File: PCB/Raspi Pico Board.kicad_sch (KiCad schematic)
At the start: 0 parts

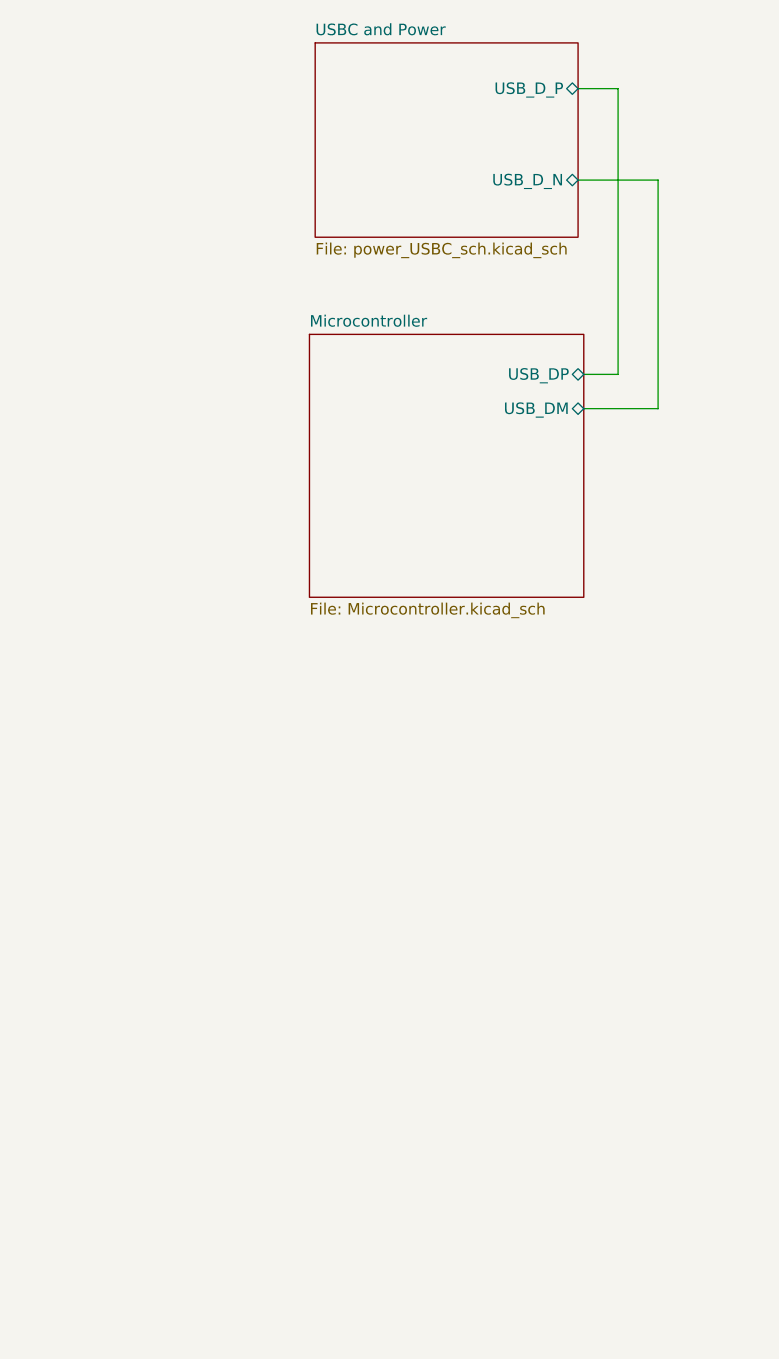
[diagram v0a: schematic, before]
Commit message: New sheet added
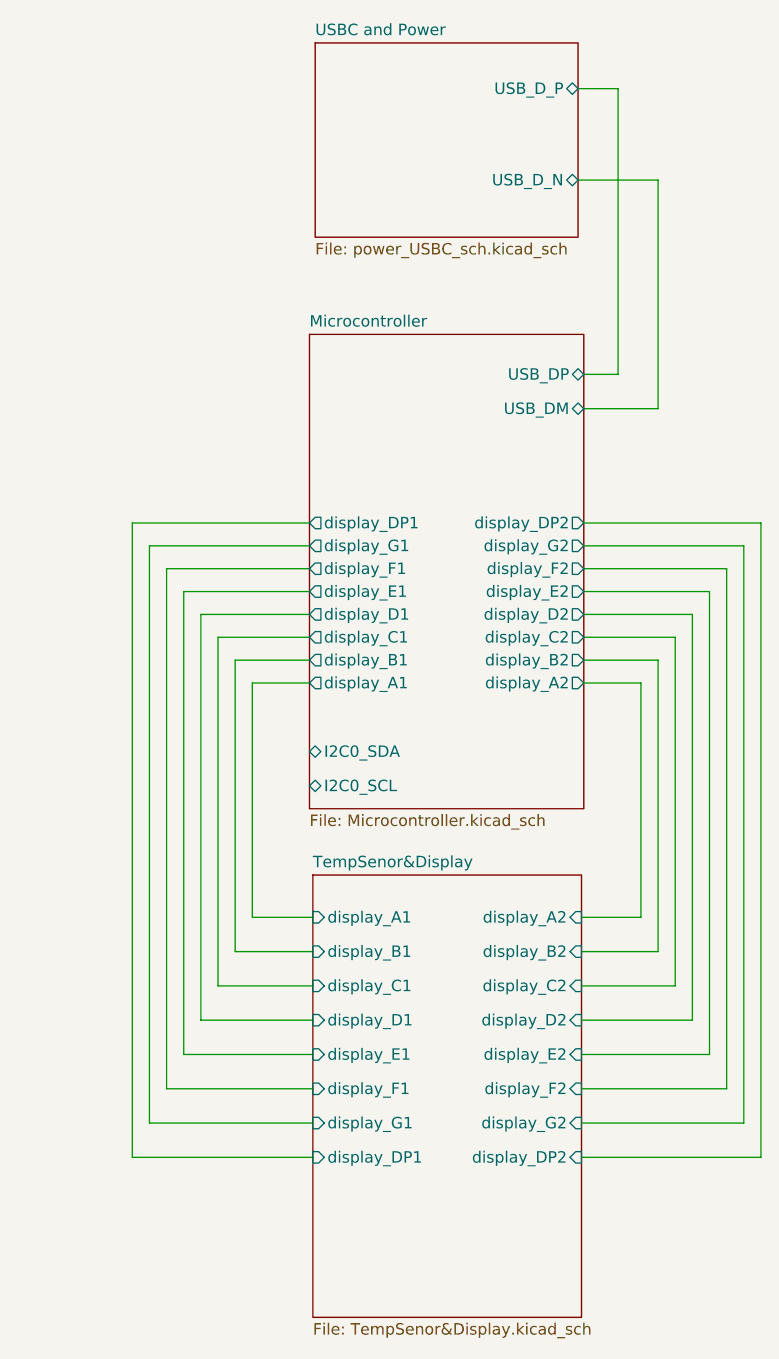
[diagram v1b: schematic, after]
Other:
- added sheet TempSenor&Display (TempSenor&Display.kicad_sch)
- sheet Microcontroller ports: added I2C0_SCL, I2C0_SDA, display_A1, display_A2, display_B1, display_B2, display_C1, display_C2, display_D1, display_D2, display_DP1, display_DP2, display_E1, display_E2, display_F1, display_F2, display_G1, display_G2; removed none

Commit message: Layout complted, gerber files generated
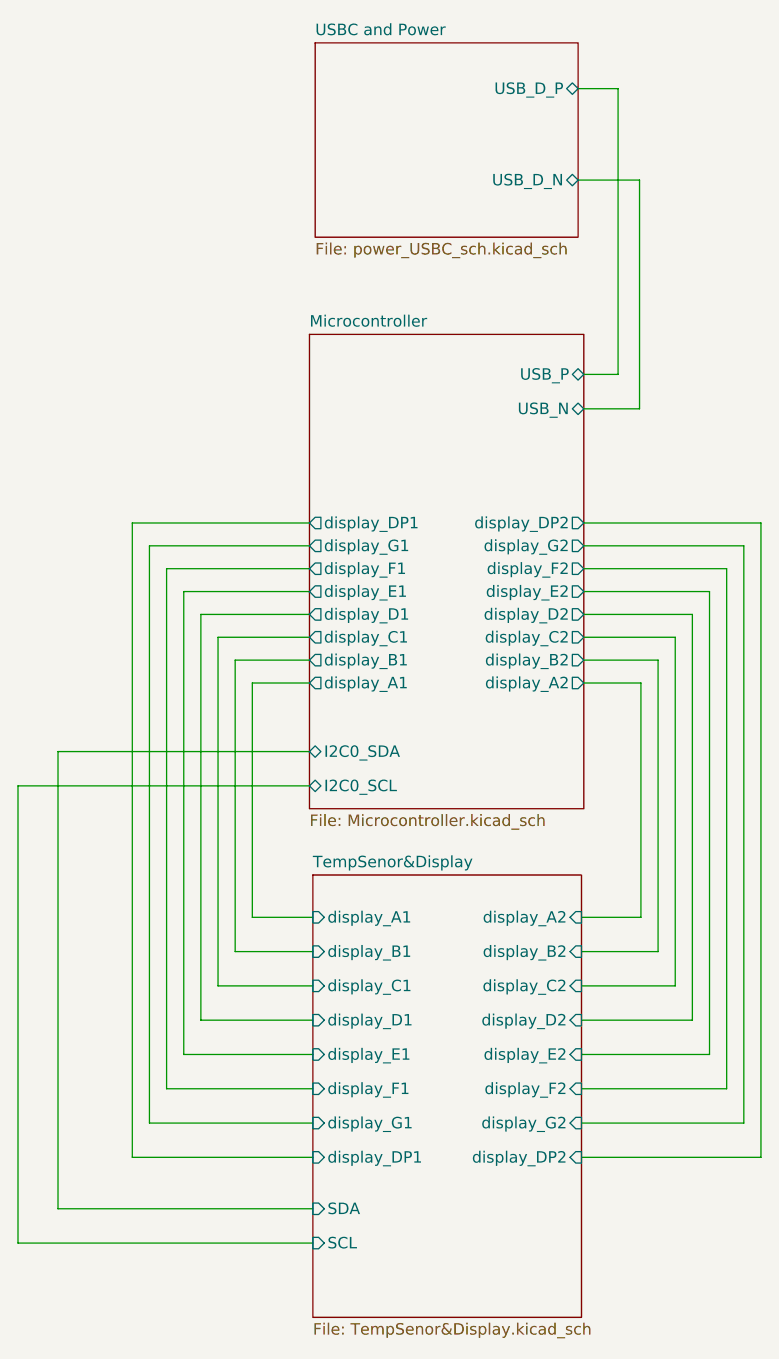
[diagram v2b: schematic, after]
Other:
- sheet Microcontroller ports: added USB_N, USB_P; removed USB_DM, USB_DP
- sheet TempSenor&Display ports: added SCL, SDA; removed none
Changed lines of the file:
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@@
+    (stroke (width 0) (type default))
+  )
+  (wire (pts (xy 95.885 108.585) (xy 95.885 159.385))
     (stroke (width 0) (type default))
   )
@@
     (stroke (width 0) (type default))
   )
-  (wire (pts (xy 153.67 45.085) (xy 162.56 45.085))
-    (stroke (width 0) (type default))
-  )
   (wire (pts (xy 160.655 100.965) (xy 160.655 127))
     (stroke (width 0) (type default))
@@
     (stroke (width 0) (type default))
   )
+  (wire (pts (xy 123.825 112.395) (xy 91.44 112.395))
+    (stroke (width 0) (type default))
+  )
+  (wire (pts (xy 153.67 45.085) (xy 160.5 45.085))
+    (stroke (width 0) (type default))
+  )
   (wire (pts (xy 170.18 88.265) (xy 170.18 146.05))
     (stroke (width 0) (type default))
@@
     (stroke (width 0) (type default))
   )
+  (wire (pts (xy 91.44 112.395) (xy 91.44 163.195))
+    (stroke (width 0) (type default))
+  )
+  (wire (pts (xy 95.885 159.385) (xy 124.206 159.385))
+    (stroke (width 0) (type default))
+  )
   (wire (pts (xy 117.475 100.965) (xy 117.475 127))
     (stroke (width 0) (type default))
@@
     (stroke (width 0) (type default))
   )
+  (wire (pts (xy 91.44 163.195) (xy 124.206 163.195))
+    (stroke (width 0) (type default))
+  )
   (wire (pts (xy 107.95 88.265) (xy 107.95 146.05))
     (stroke (width 0) (type default))
@@
     (stroke (width 0) (type default))
   )
+  (wire (pts (xy 160.5 45.085) (xy 160.5 70.5))
+    (stroke (width 0) (type default))
+  )
   (wire (pts (xy 107.95 146.05) (xy 124.206 146.05))
     (stroke (width 0) (type default))
@@
     (stroke (width 0) (type default))
   )
-  (wire (pts (xy 162.56 45.085) (xy 162.56 70.485))
-    (stroke (width 0) (type default))
-  )
   (wire (pts (xy 158.115 34.925) (xy 158.115 66.675))
     (stroke (width 0) (type default))
@@
     (stroke (width 0) (type default))
   )
+  (wire (pts (xy 160.5 70.5) (xy 154.305 70.5))
+    (stroke (width 0) (type default))
+  )
   (wire (pts (xy 162.56 130.81) (xy 154.051 130.81))
     (stroke (width 0) (type default))
@@
     (stroke (width 0) (type default))
   )
-  (wire (pts (xy 154.305 70.485) (xy 162.56 70.485))
-    (stroke (width 0) (type default))
-  )
   (wire (pts (xy 170.18 146.05) (xy 154.051 146.05))
+    (stroke (width 0) (type default))
+  )
+  (wire (pts (xy 123.825 108.585) (xy 95.885 108.585))
     (stroke (width 0) (type default))
   )
@@
       (effects (font (size 1.27 1.27)) (justify left top))
     )
-    (pin "USB_DP" bidirectional (at 154.305 66.675 0)
-      (effects (font (size 1.27 1.27)) (justify right))
-    )
-    (pin "USB_DM" bidirectional (at 154.305 70.485 0)
-      (effects (font (size 1.27 1.27)) (justify right))
-    )
     (pin "display_B1" output (at 123.825 98.425 180)
       (effects (font (size 1.27 1.27)) (justify left))
@@
     )
     (pin "display_DP2" output (at 154.305 83.185 0)
+      (effects (font (size 1.27 1.27)) (justify right))
+    )
+    (pin "USB_P" bidirectional (at 154.305 66.675 0)
+      (effects (font (size 1.27 1.27)) (justify right))
+    )
+    (pin "USB_N" bidirectional (at 154.305 70.5 0)
       (effects (font (size 1.27 1.27)) (justify right))
     )
@@
       (effects (font (size 1.27 1.27)) (justify left))
     )
+    (pin "SDA" input (at 124.206 159.385 180)
+      (effects (font (size 1.27 1.27)) (justify left))
+    )
+    (pin "SCL" input (at 124.206 163.195 180)
+      (effects (font (size 1.27 1.27)) (justify left))
+    )
